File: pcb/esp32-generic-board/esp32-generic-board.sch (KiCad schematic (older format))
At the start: 24 parts, among them J1 USB_C_Receptacle, J2 WAGO_2060-451_998-404, J3 Conn_01x19, J4 Conn_01x19, U1 MIC5219-3.3YM5, U2 LTC3630MSE, U3 FT232RL, U4 ESP32-WROOM-32

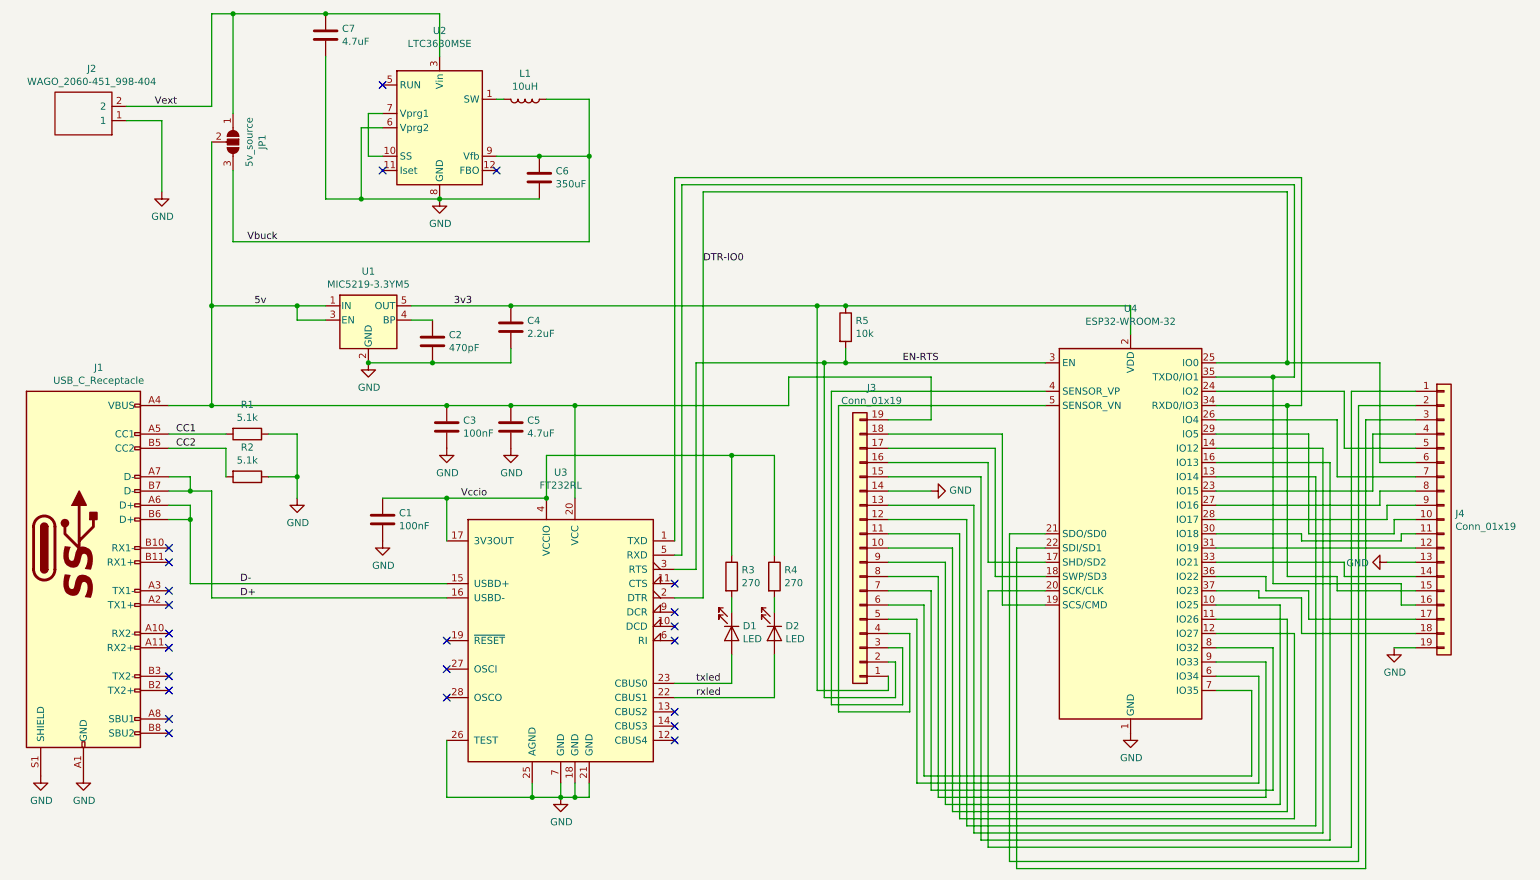
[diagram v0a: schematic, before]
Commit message: Version 2 with switch from FTDI to WCH CH340C USB-UART IC
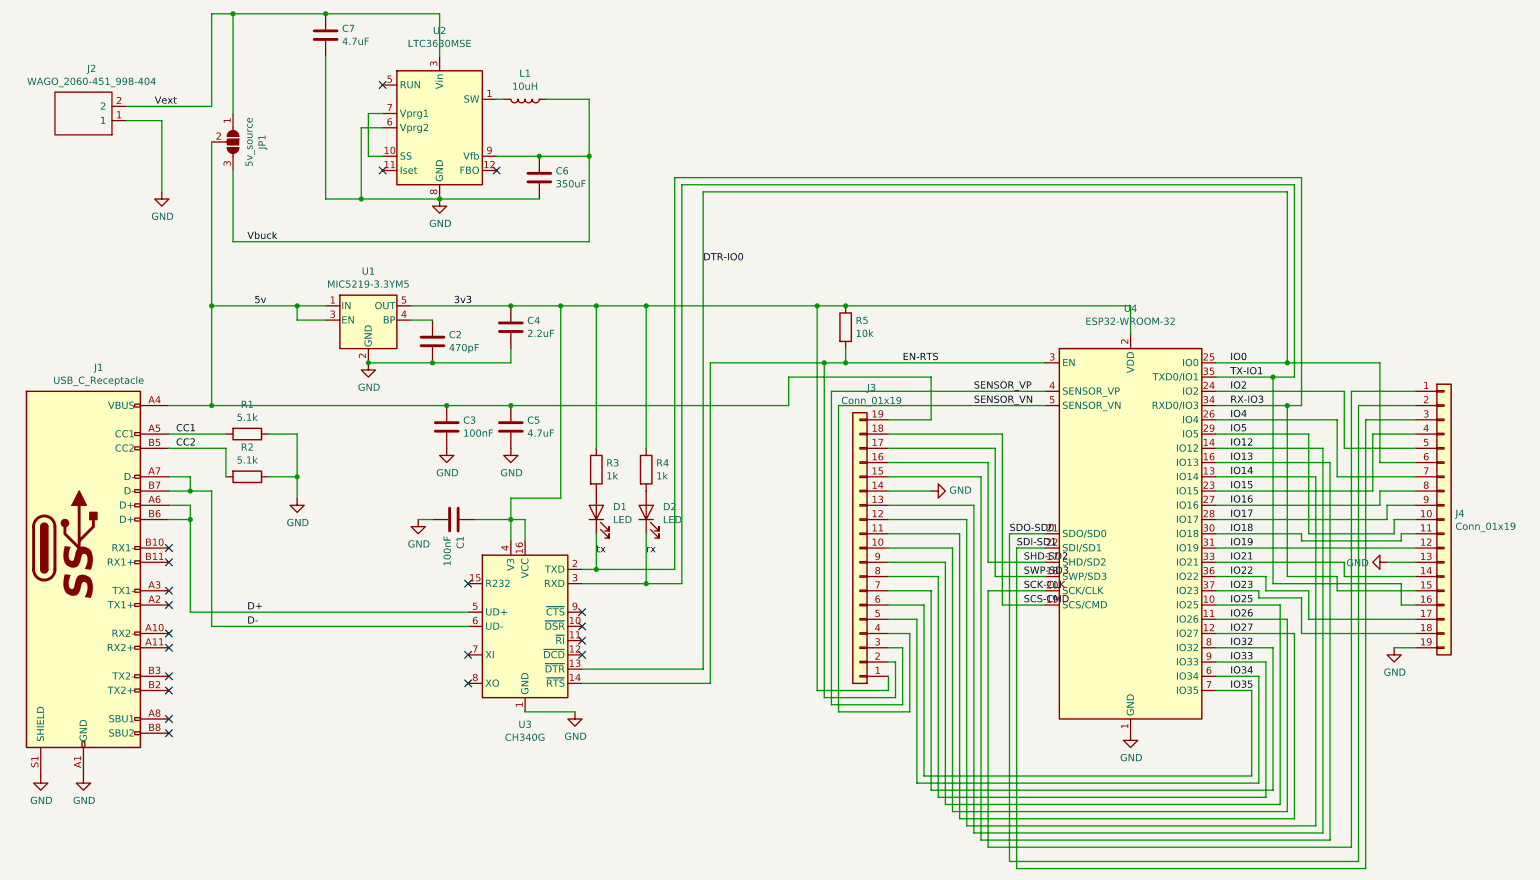
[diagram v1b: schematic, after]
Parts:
- removed U3: FT232RL, Package_SO:SSOP-28_5.3x10.2mm_P0.65mm, symbol Interface_USB:FT232RL
- added U3: CH340G, Package_SO:SOIC-16_3.9x9.9mm_P1.27mm, symbol Interface_USB:CH340G
- R3, R4: value 270 -> 1k
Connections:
- net Vccio is gone; now on net 3v3: C1.1, R3.1, R4.1
- net rxled is gone; now on an unnamed net: D2.2 (A)
- net txled is gone; now on an unnamed net: D1.2 (A)
- net 3v3: now also U3.16 (VCC), U3.4 (V3)
- net D+: now also J1.A6 (D+), J1.B6 (D+), U3.5 (UD+); no longer J1.A7 (D-), J1.B7 (D-)
- net D-: now also J1.A7 (D-), J1.B7 (D-), U3.6 (UD-); no longer J1.A6 (D+), J1.B6 (D+)
- net DTR-IO0: now also U3.13 (~DTR)
- net EN-RTS: now also U3.14 (~RTS)
- net GND: now also U3.1 (GND)
- net IO25: now reaches J3.9 (Pin_9), U4.10 (IO25)
- net IO26: now reaches J3.10 (Pin_10), U4.11 (IO26)
- net IO27: now reaches J3.11 (Pin_11), U4.12 (IO27)
- net IO14: now reaches J3.12 (Pin_12), U4.13 (IO14)
- net IO12: now reaches J3.13 (Pin_13), U4.14 (IO12)
- net IO13: now reaches J3.15 (Pin_15), U4.16 (IO13)
- net SHD-SD2: now reaches J3.16 (Pin_16), U4.17 (SHD/SD2)
- net SWP-SD3: now reaches J3.17 (Pin_17), U4.18 (SWP/SD3)
- net SCS-CMD: now reaches J3.18 (Pin_18), U4.19 (SCS/CMD)
- net SCK-CLK: now reaches J4.1 (Pin_1), U4.20 (SCK/CLK)
- net SDO-SD0: now reaches J4.2 (Pin_2), U4.21 (SDO/SD0)
- net SDI-SD1: now reaches J4.3 (Pin_3), U4.22 (SDI/SD1)
- net IO15: now reaches J4.4 (Pin_4), U4.23 (IO15)
- net IO2: now reaches J4.5 (Pin_5), U4.24 (IO2)
- net IO4: now reaches J4.7 (Pin_7), U4.26 (IO4)
- net IO16: now reaches J4.8 (Pin_8), U4.27 (IO16)
- net IO17: now reaches J4.9 (Pin_9), U4.28 (IO17)
- net IO5: now reaches J4.10 (Pin_10), U4.29 (IO5)
- net IO18: now reaches J4.11 (Pin_11), U4.30 (IO18)
- net IO19: now reaches J4.12 (Pin_12), U4.31 (IO19)
- net IO21: now reaches J4.14 (Pin_14), U4.33 (IO21)
- net RX-IO3: now reaches J4.15 (Pin_15), U4.34 (RXD0/IO3)
- net RX-IO3: now also D1.1 (K), U3.2 (TXD)
- net TX-IO1: now reaches J4.16 (Pin_16), U4.35 (TXD0/IO1)
- net TX-IO1: now also D2.1 (K), U3.3 (RXD)
- net IO22: now reaches J4.17 (Pin_17), U4.36 (IO22)
- net IO23: now reaches J4.18 (Pin_18), U4.37 (IO23)
- net SENSOR_VP: now reaches J3.3 (Pin_3), U4.4 (SENSOR_VP)
- net SENSOR_VN: now reaches J3.4 (Pin_4), U4.5 (SENSOR_VN)
- net IO34: now reaches J3.5 (Pin_5), U4.6 (IO34)
- net IO35: now reaches J3.6 (Pin_6), U4.7 (IO35)
- net IO32: now reaches J3.7 (Pin_7), U4.8 (IO32)
- net IO33: now reaches J3.8 (Pin_8), U4.9 (IO33)
- net at R3.2: no longer D1.1 (K)
- net at R4.2: no longer D2.1 (K)
- no-connect marks 23 -> 20
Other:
- moved on the sheet: C1
